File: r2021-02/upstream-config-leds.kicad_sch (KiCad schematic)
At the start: 82 parts, among them J1 Conn_01x06, J5 Conn_01x03_Male, J8 USB_A male UP, J9 USB_B_Micro (up), Q1 Si4435, U1 2k i2c eeprom, U12 NUP4202, U18 SY8366H, U2 SE5120ST33, U3 USB2517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

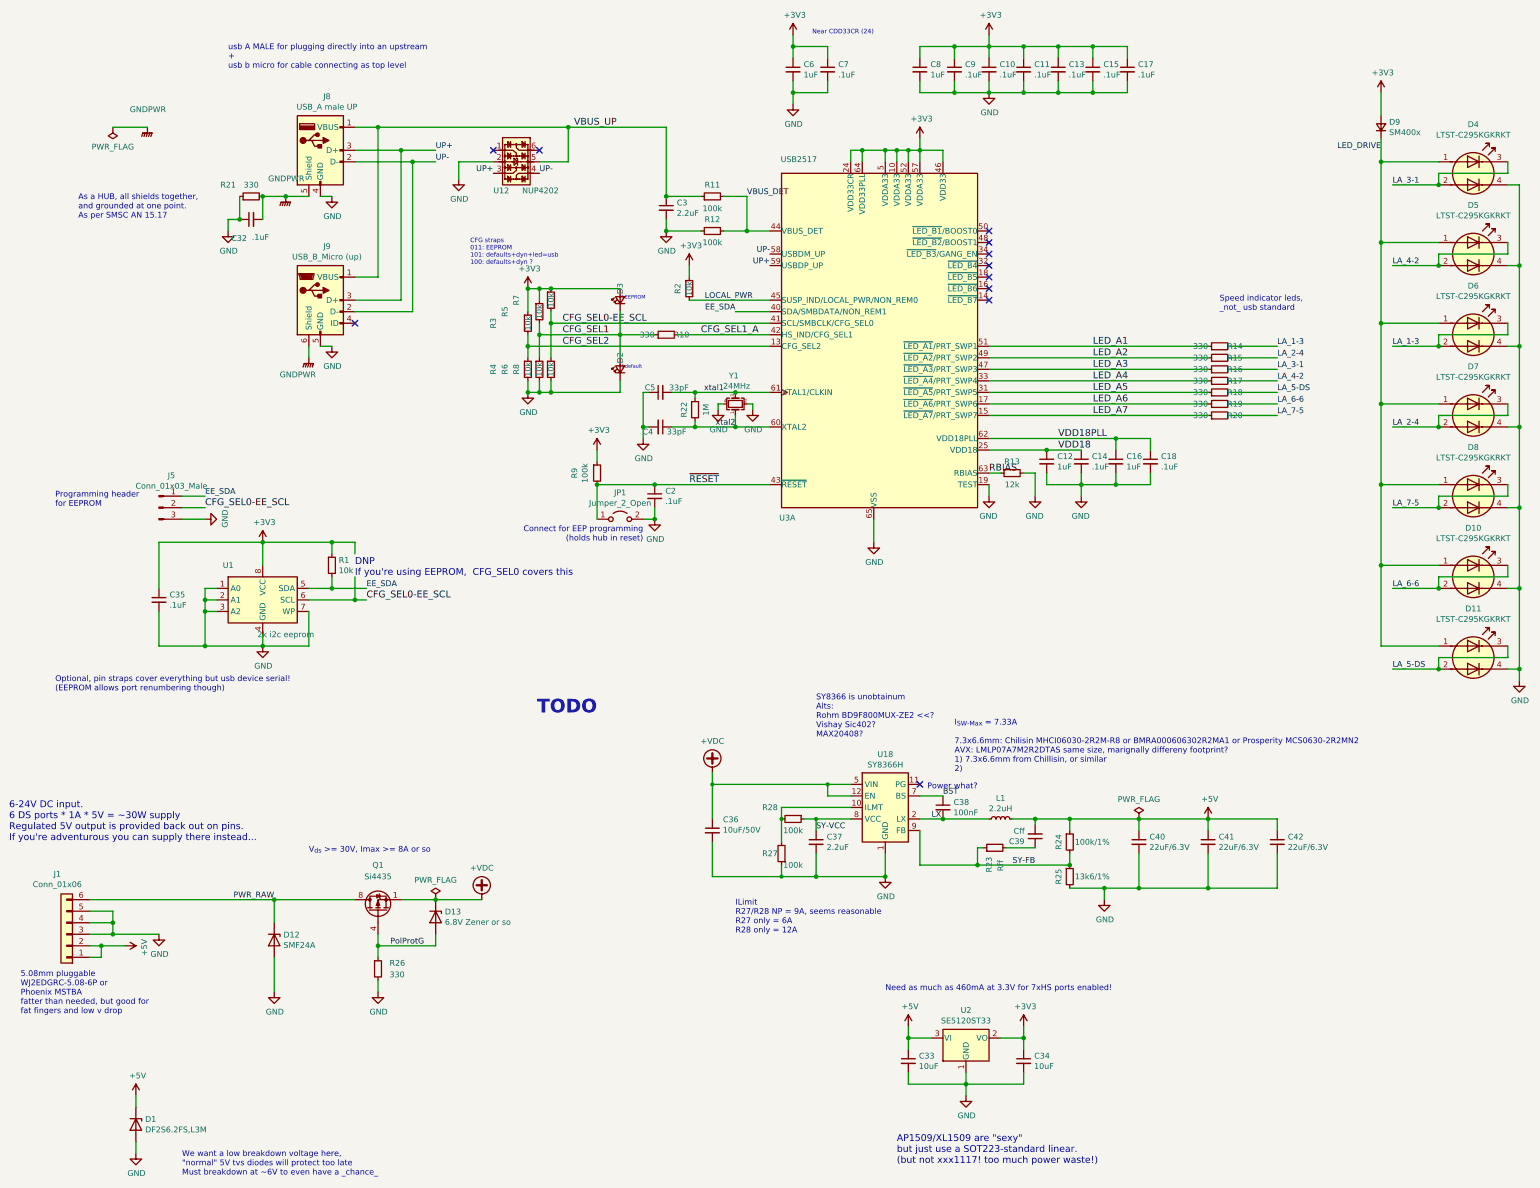
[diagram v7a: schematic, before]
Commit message: hw-rev2: break out power input to a new sheet
It was always a bit crowded there, and now that we need to pick new
parts, we want a little more space...
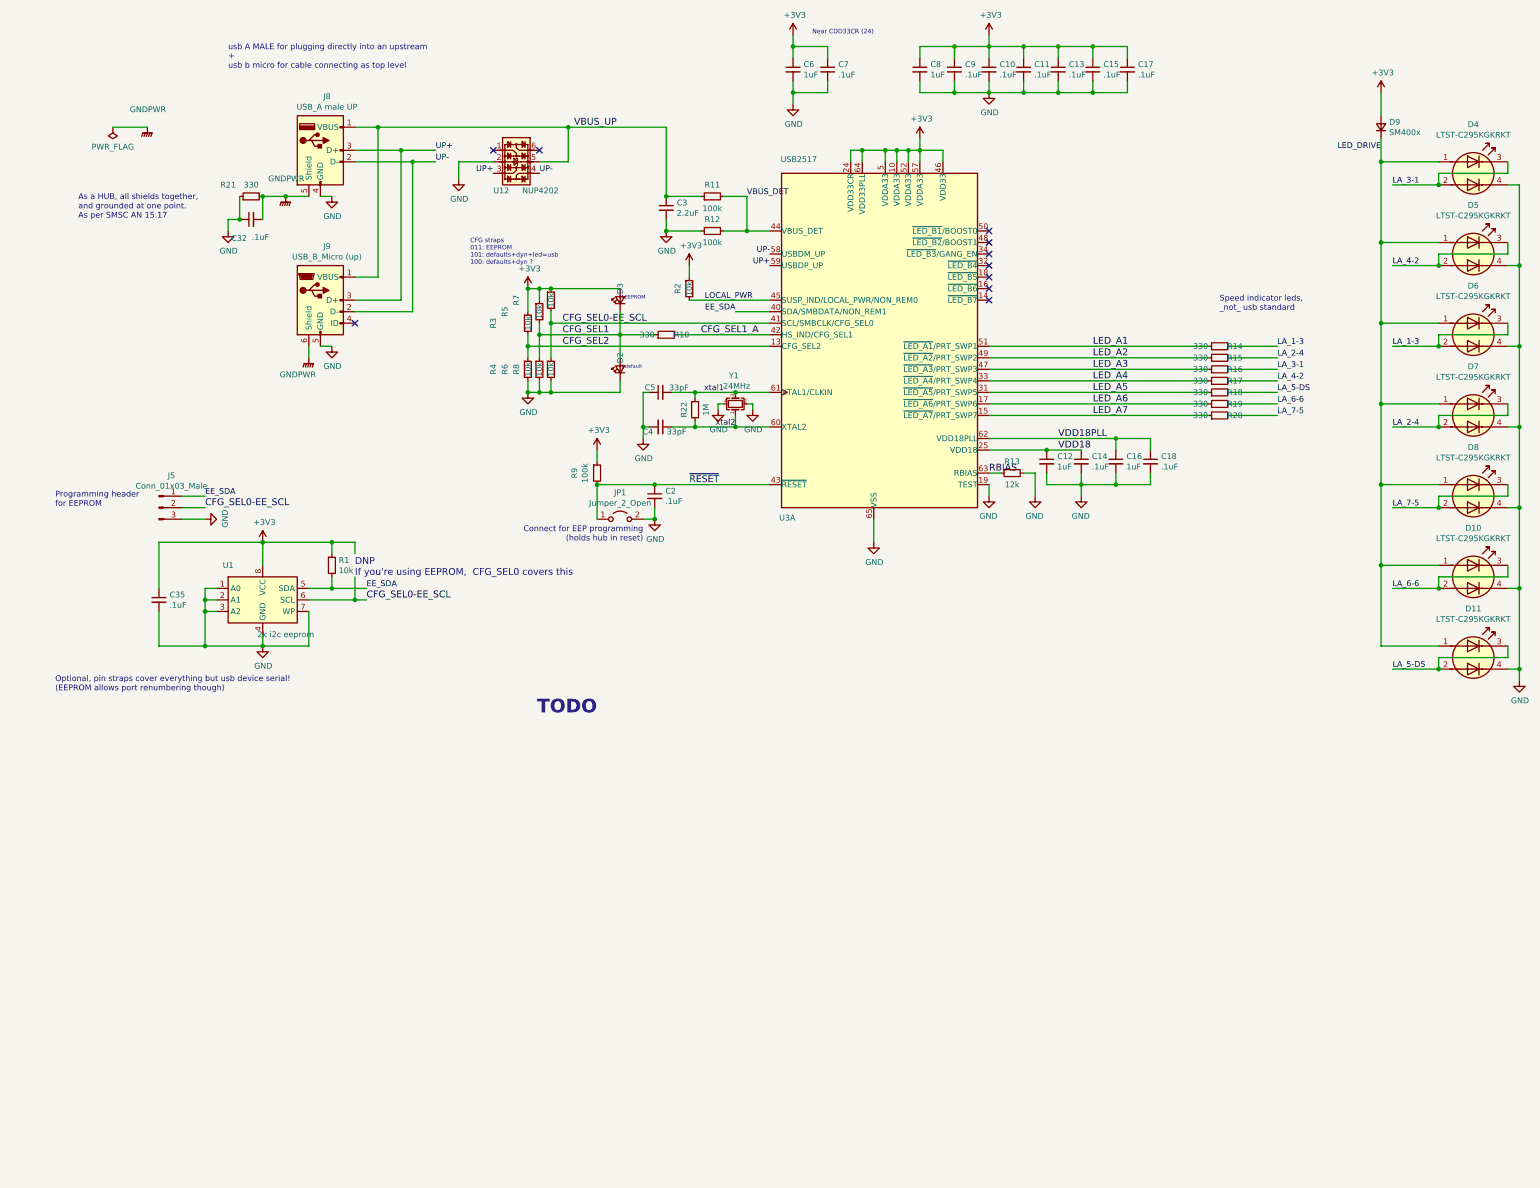
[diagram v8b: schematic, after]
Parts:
- removed C33, C34: 10uF, Capacitor_SMD:C_0805_2012Metric, symbol Device:C_Small
- removed C36: 10uF/50V, Capacitor_SMD:C_0805_2012Metric, symbol Device:C_Small
- removed C37: 2.2uF, Capacitor_SMD:C_0603_1608Metric, symbol Device:C_Small
- removed C38: 100nF, Capacitor_SMD:C_0603_1608Metric, symbol Device:C_Small
- removed C39: Cff, Capacitor_SMD:C_0603_1608Metric, symbol Device:C_Small
- removed C40, C41, C42: 22uF/6.3V, Capacitor_SMD:C_0805_2012Metric, symbol Device:C_Small
- removed D1: DF2S6.2FS,L3M, Diode_SMD:D_SOD-923, symbol Device:D_Zener
- removed D12: SMF24A, Diode_SMD:D_SOD-123F, symbol Device:D_Zener
- removed D13: 6.8V Zener or so, Diode_SMD:D_SOD-123F, symbol Device:D_Zener
- removed J1: Conn_01x06, Connector_Phoenix_MSTB:PhoenixContact_MSTBA_2,5_6-G-5,08_1x06_P5.08mm_Horizontal, symbol Connector_Generic:Conn_01x06
- removed L1: 2.2uH, Inductor_SMD:L_CHILISIN_BMRx00060630, symbol Device:L_Small
- removed Q1: Si4435, Package_SO:SOIC-8_3.9x4.9mm_P1.27mm, symbol Transistor_FET:IRF7404
- removed R23: Rff, Resistor_SMD:R_0603_1608Metric, symbol Device:R_Small
- removed R24: 100k/1%, Resistor_SMD:R_0603_1608Metric, symbol Device:R_Small
- removed R25: 13k6/1%, Resistor_SMD:R_0603_1608Metric, symbol Device:R_Small
- removed R26: 330, Resistor_SMD:R_0603_1608Metric, symbol Device:R_Small
- removed R27, R28: 100k, Resistor_SMD:R_0603_1608Metric, symbol Device:R_Small
- removed U18: SY8366H, et-parts:SY8366H, symbol etactica-parts:SY8366H
- removed U2: SE5120ST33, Package_TO_SOT_SMD:SOT-223-3_TabPin2, symbol Regulator_Linear:AMS1117-3.3
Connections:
- no-connect marks 11 -> 10
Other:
- note removed: "5.08mm pluggable WJ2EDGRC-5.08-6P or Phoenix MSTBA fatter than needed, but good for fat fingers and low v drop"
- note removed: "6-24V DC input. 6 DS ports * 1A * 5V = ~30W supply Regulated 5V output is provided back out on pins. If you're adventurous you can supply there instead..."
- note removed: "AP1509/XL1509 are "sexy" but just use a SOT223-standard linear. (but not xxx1117! too much power waste!)"
- note removed: "ILimit R27/R28 NP = 9A, seems reasonable R27 only = 6A R28 only = 12A"
- note removed: "I_{SW-Max} = 7.33A 7.3x6.6mm: Chilisin MHCI06030-2R2M-R8 or BMRA000606302R2MA1 or Prosperity MCS0630-2R2MN2 AVX: LMLP07A7M2R2DTAS same size, marignally differeny footprint? 1) 7.3x6.6mm from Chillisin, or similar 2)"
- note removed: "Need as much as 460mA at 3.3V for 7xHS ports enabled!"
- note removed: "Power what?"
- note removed: "SY8366 is unobtainum Alts: Rohm BD9F800MUX-ZE2 <<? Vishay Sic402? MAX20408?"
- note removed: "V_{ds} >= 30V, Imax >= 8A or so"
- note removed: "We want a low breakdown voltage here, "normal" 5V tvs diodes will protect too late Must breakdown at ~6V to even have a _chance_"
